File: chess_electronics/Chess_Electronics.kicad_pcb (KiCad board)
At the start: 4 copper layers, 217.5 x 172.5 mm, 84 parts, among them J1 Screw_Terminal_01x16, J2 Screw_Terminal_01x16, J3 Screw_Terminal_01x16, J4 Screw_Terminal_01x16, J5 Screw_Terminal_01x16, J6 Screw_Terminal_01x16, J7 Screw_Terminal_01x16, J8 Screw_Terminal_01x16, J9 Barrel_Jack, U1 SN74LV4051AN, U2 SN74LV4051AN, U3 SN74LV4051AN, U4 SN74LV4051AN, U5 SN74LV4051AN, U6 SN74LV4051AN, U7 SN74LV4051AN, U8 SN74LV4051AN

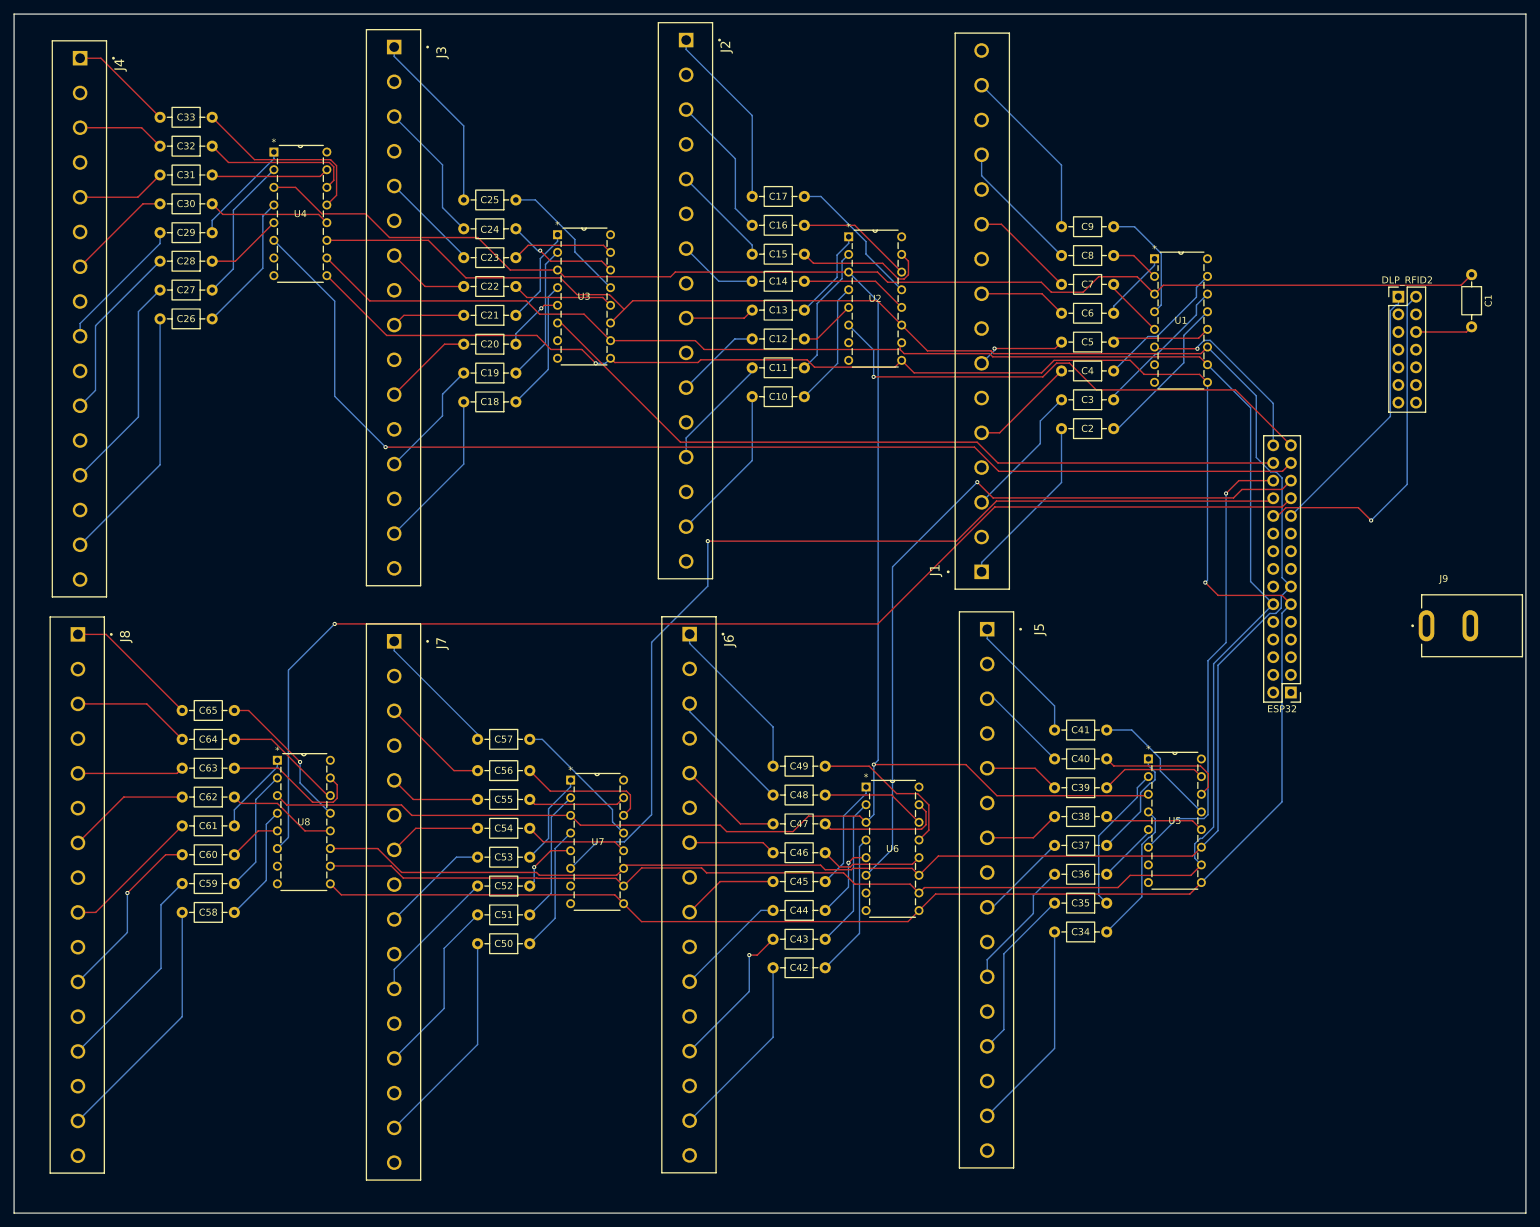
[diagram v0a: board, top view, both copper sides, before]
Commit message: Update PCB to use two multiplexers by chaining signal and ground in opposite directions
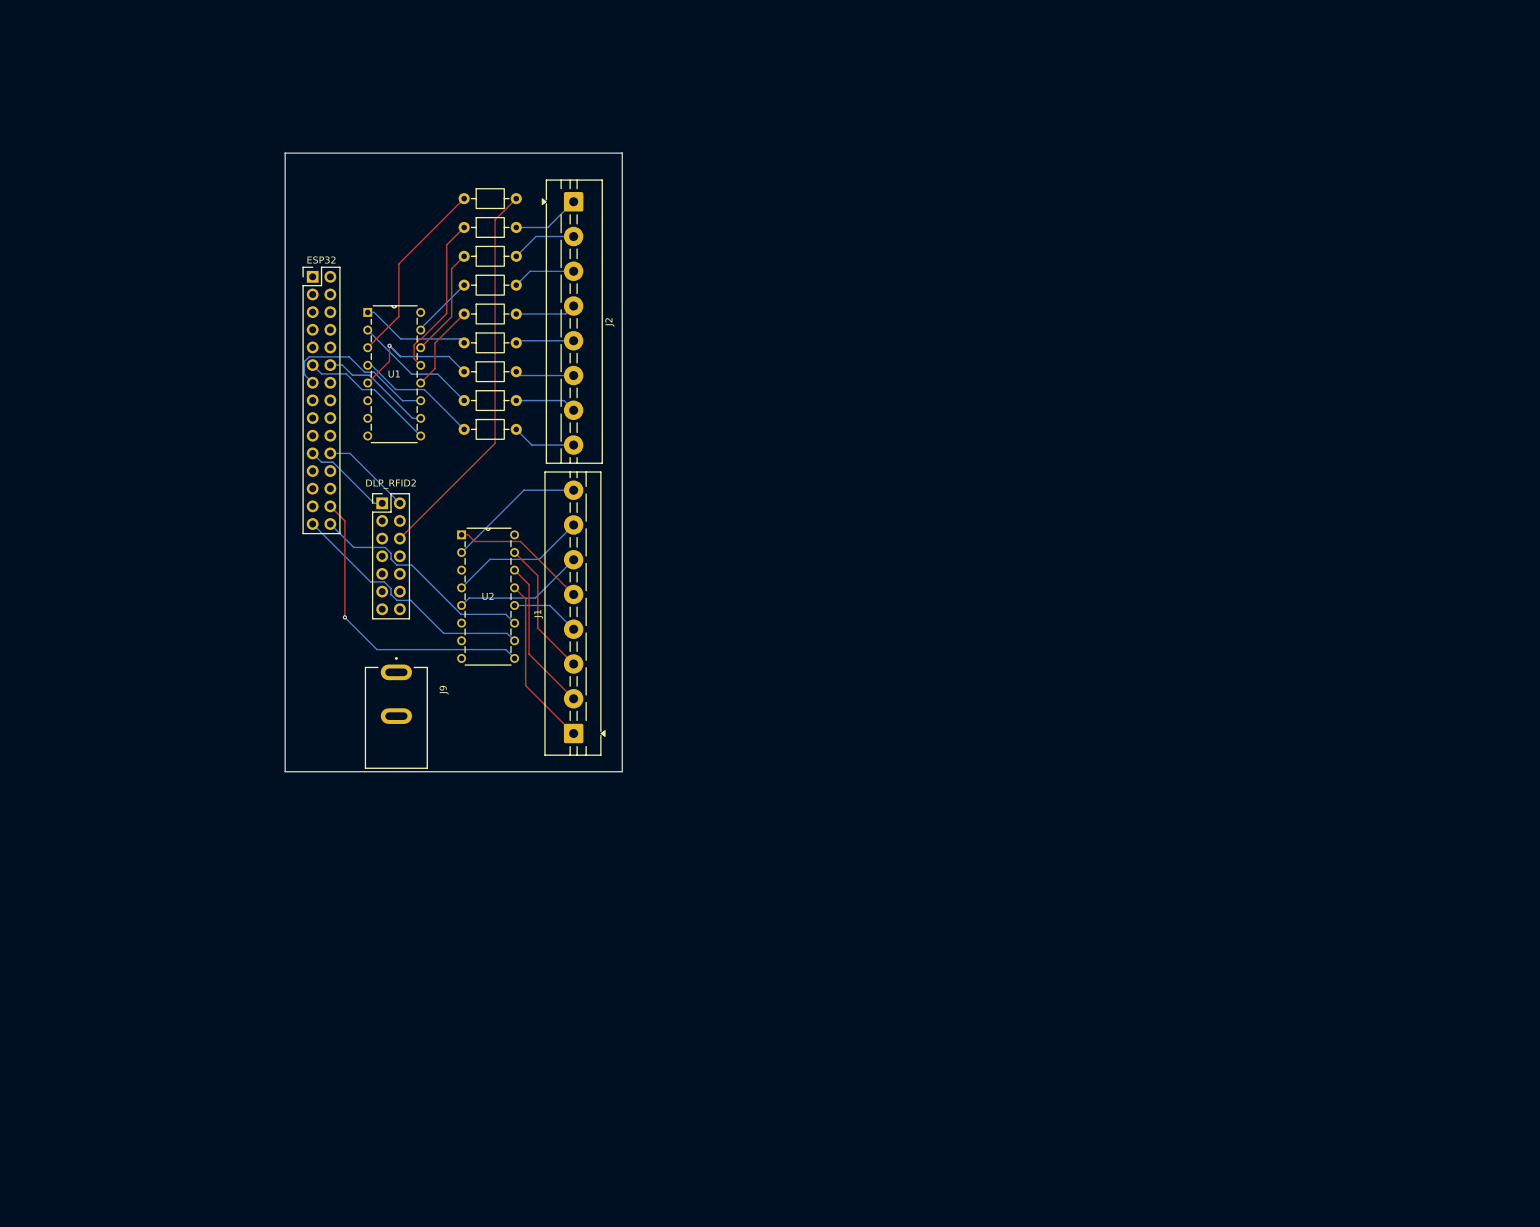
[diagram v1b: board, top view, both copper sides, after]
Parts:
- removed C10, C11, C12, C13, C14, C15, C16, C17, C18, C19, C20, C21, C22, C23, C24, C25, C26, C27, C28, C29, C30, C31, C32, C33, C34, C35, C36, C37, C38, C39, C40, C41, C42, C43, C44, C45, C46, C47, C48, C49, C50, C51, C52, C53, C54, C55, C56, C57, C58, C59, C60, C61, C62, C63, C64, C65: C_Small_US, Capacitor_THT:C_Axial_L3.8mm_D2.6mm_P7.50mm_Horizontal
- removed J3, J4, J5, J6, J7, J8: Screw_Terminal_01x16, KiCad:CUI_TB003-500-P16BE
- removed U3, U4, U5, U6, U7, U8: SN74LV4051AN, KiCad:N16
- J1, J2: value Screw_Terminal_01x16 -> Screw_Terminal_01x08; footprint KiCad:CUI_TB003-500-P16BE -> TerminalBlock:TerminalBlock_MaiXu_MX126-5.0-08P_1x08_P5.00mm
- moved ESP32 152.9 mm to (74.0, 49.3), turned to 0 degrees
- moved DLP_RFID2 149.2 mm to (84.0, 81.9)
- moved J9 148.4 mm to (86.0, 106.2), turned to -90 degrees
- moved C1 145.4 mm to (95.8, 38.0), turned to 0 degrees
- moved U1 113.5 mm to (89.5, 72.2)
- moved C9 97.9 mm to (95.8, 71.2), turned to 0 degrees
- moved C2 97.8 mm to (95.8, 42.2), turned to 0 degrees
- moved C8 95.7 mm to (95.8, 67.1), turned to 0 degrees
- moved C3 95.7 mm to (95.8, 46.4), turned to 0 degrees
- moved C7 94.3 mm to (95.8, 63.0), turned to 0 degrees
- moved C4 94.3 mm to (95.8, 50.5), turned to 0 degrees
- moved C6 93.5 mm to (95.8, 58.8), turned to 0 degrees
- moved C5 93.5 mm to (95.8, 54.6), turned to 0 degrees
- moved U2 70.3 mm to (103.0, 104.2)
- moved J1 63.1 mm to (111.5, 115.0)
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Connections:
- C2 pad 2: Net-(J1-Pin_1) -> Net-(J2-Pin_1)
- C3 pad 2: Net-(J1-Pin_3) -> Net-(J2-Pin_2)
- C4 pad 2: Net-(J1-Pin_5) -> Net-(J2-Pin_3)
- C5 pad 2: Net-(J1-Pin_7) -> Net-(J2-Pin_4)
- C6 pad 2: Net-(J1-Pin_9) -> Net-(J2-Pin_5)
- C7 pad 2: Net-(J1-Pin_11) -> Net-(J2-Pin_6)
- C8 pad 2: Net-(J1-Pin_13) -> Net-(J2-Pin_7)
- C9 pad 2: Net-(J1-Pin_15) -> Net-(J2-Pin_8)
- ESP32 pad 23: Mux8 INH -> unconnected-(ESP32-Pin_23-Pad23)
- ESP32 pad 24: Mux7 INH -> unconnected-(ESP32-Pin_24-Pad24)
- ESP32 pad 25: Mux6 INH -> unconnected-(ESP32-Pin_25-Pad25)
- ESP32 pad 26: Mux5 INH -> unconnected-(ESP32-Pin_26-Pad26)
- ESP32 pad 27: Mux4 INH -> unconnected-(ESP32-Pin_27-Pad27)
- ESP32 pad 28: Mux3 INH -> F
- ESP32 pad 29: Mux2 INH -> E
- ESP32 pad 30: Mux1 INH -> D
- J1 pad 2: GND -> Net-(J1-Pin_2)
- J1 pad 4: GND -> Net-(J1-Pin_4)
- J1 pad 6: GND -> Net-(J1-Pin_6)
- J1 pad 8: GND -> Net-(J1-Pin_8)
- J2 pad 2: GND -> Net-(J2-Pin_2)
- J2 pad 4: GND -> Net-(J2-Pin_4)
- J2 pad 6: GND -> Net-(J2-Pin_6)
- J2 pad 8: GND -> Net-(J2-Pin_8)
- U1 pad 6: Mux1 INH -> unconnected-(U1-INH-Pad6)
- U2 pad 1: Net-(U2-Y4) -> Net-(J1-Pin_5)
- U2 pad 10: B -> E
- U2 pad 11: A -> D
- U2 pad 12: Net-(U2-Y3) -> Net-(J1-Pin_4)
- U2 pad 13: Net-(U2-Y0) -> Net-(J1-Pin_1)
- U2 pad 14: Net-(U2-Y1) -> Net-(J1-Pin_2)
- U2 pad 15: Net-(U2-Y2) -> Net-(J1-Pin_3)
- U2 pad 2: Net-(U2-Y6) -> Net-(J1-Pin_8)
- U2 pad 3: Common -> GND
- U2 pad 4: Net-(U2-Y7) -> Net-(J1-Pin_7)
- U2 pad 5: Net-(U2-Y5) -> Net-(J1-Pin_6)
- U2 pad 6: Mux2 INH -> unconnected-(U2-INH-Pad6)
- U2 pad 9: C -> F
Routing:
- net Common: track 393.4 -> 27.2 mm, vias 1 -> 0
- net C: track 354.1 -> 19.8 mm, vias 2 -> 0
- net B: track 346.0 -> 16.2 mm
- net A: track 350.8 -> 23.1 mm
- net Mux8 INH: track 180.8 -> 0.00 mm, vias 1 -> 0
- net Mux4 INH: track 168.6 -> 0.00 mm, vias 1 -> 0
- net Mux7 INH: track 141.4 -> 0.00 mm, vias 1 -> 0
- net Mux3 INH: track 111.3 -> 0.00 mm
- net Mux6 INH: track 110.3 -> 0.00 mm, vias 1 -> 0
- net Mux2 INH: track 74.7 -> 0.00 mm, vias 1 -> 0
- net Mux5 INH: track 65.4 -> 0.00 mm, vias 1 -> 0
- net Net-(DLP_RFID2-Pin_6): track 8.31 -> 55.8 mm
- net F: track 0.00 -> 43.7 mm, vias 0 -> 1
- net Net-(J4-Pin_15): track 37.3 -> 0.00 mm
- net TXD From ESP32: track 50.2 -> 13.0 mm, vias 1 -> 0
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- added copper zone on In1.Cu, net +5V
- added copper zone on In2.Cu, net GND
- removed copper zone on In2.Cu, net +5V
- removed copper zone on In1.Cu, net GND
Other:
- board size 217.5 x 172.5 mm -> 48.5 x 89 mm
